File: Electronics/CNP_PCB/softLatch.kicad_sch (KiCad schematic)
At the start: 10 parts, among them Q2 Q_NMOS_GSD, Q3 Q_NMOS_GSD, Q5 Q_PMOS_GSD, SW1 SW_SPST

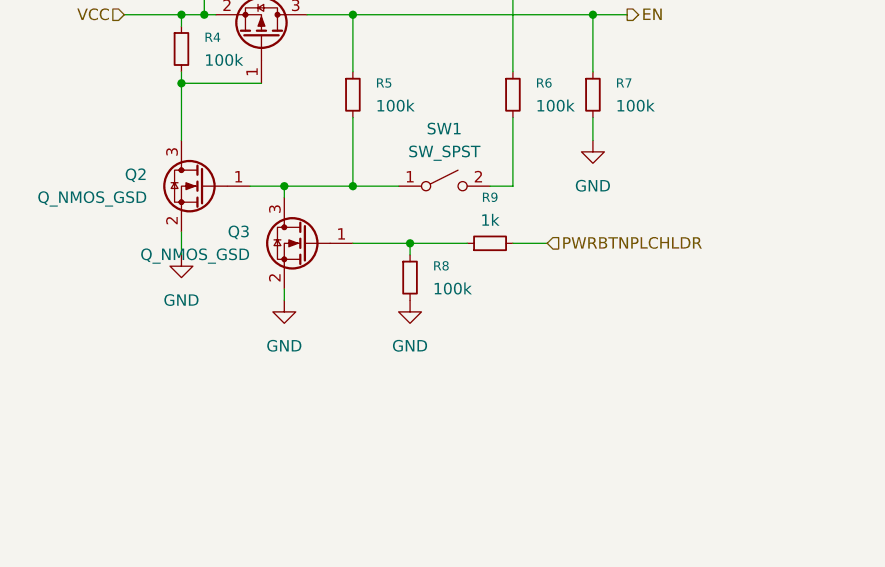
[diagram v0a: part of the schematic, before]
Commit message: finished softLatch circuit
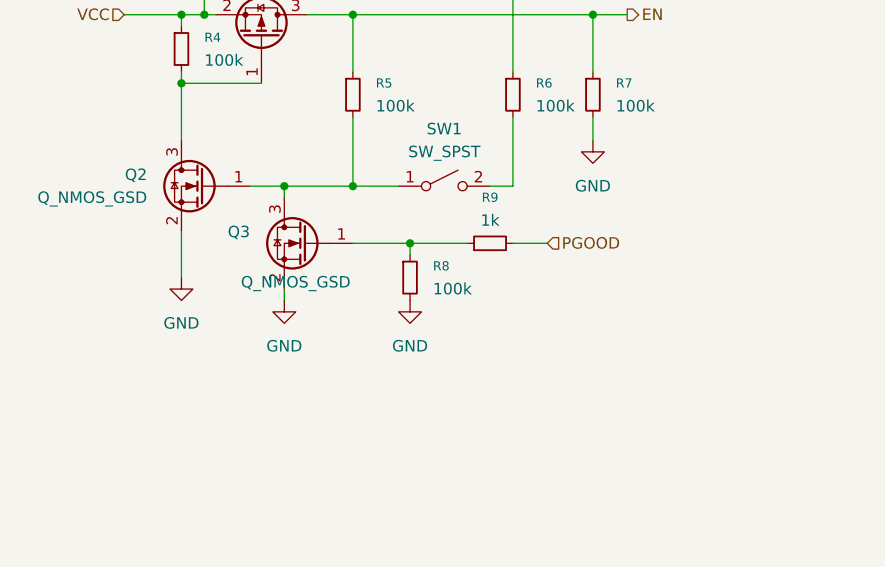
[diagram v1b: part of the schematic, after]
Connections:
- net PWRBTNPLCHLDR renamed PGOOD
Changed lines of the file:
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@@
 	(wire
 		(pts
-			(xy 137.16 76.2) (xy 137.16 73.66)
+			(xy 137.16 78.74) (xy 137.16 73.66)
 		)
 		(stroke
@@
 		)
 	)
-	(hierarchical_label "PWRBTNPLCHLDR"
+	(hierarchical_label "PGOOD"
 		(shape input)
 		(at 177.8 74.93 0)
@@
 		(on_board yes)
 		(dnp no)
-		(fields_autoplaced yes)
 		(property "Reference" "Q3"
 			(at 144.78 73.6599 0)
@@
 		)
 		(property "Value" "Q_NMOS_GSD"
-			(at 144.78 76.1999 0)
+			(at 155.956 79.248 0)
 			(effects
 				(font
@@
 	(symbol
 		(lib_id "power:GND")
-		(at 137.16 76.2 0)
+		(at 137.16 78.74 0)
 		(unit 1)
 		(exclude_from_sim no)
@@
 		(fields_autoplaced yes)
 		(property "Reference" "#PWR010"
-			(at 137.16 82.55 0)
+			(at 137.16 85.09 0)
 			(effects
 				(font
@@
 		)
 		(property "Value" "GND"
-			(at 137.16 81.28 0)
+			(at 137.16 83.82 0)
 			(effects
 				(font
@@
 		)
 		(property "Footprint" ""
-			(at 137.16 76.2 0)
+			(at 137.16 78.74 0)
 			(effects
 				(font
@@
 		)
 		(property "Datasheet" ""
-			(at 137.16 76.2 0)
+			(at 137.16 78.74 0)
 			(effects
 				(font
@@
 		)
 		(property "Description" "Power symbol creates a global label with name \"GND\" , ground"
-			(at 137.16 76.2 0)
-			(effects
-				(font
+			(at 137.16 78.74 0)
+			(effects
+				(font

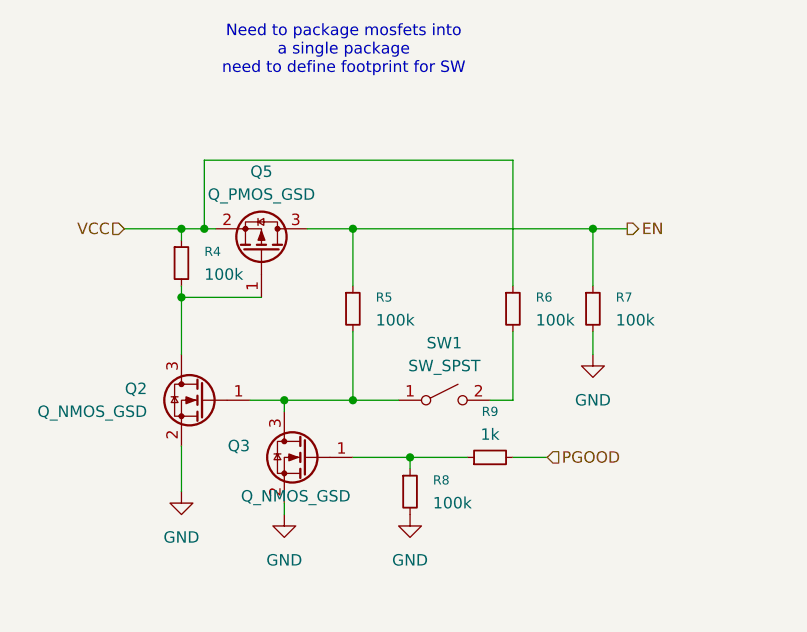
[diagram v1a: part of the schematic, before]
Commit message: added switch logic for emulating buttons
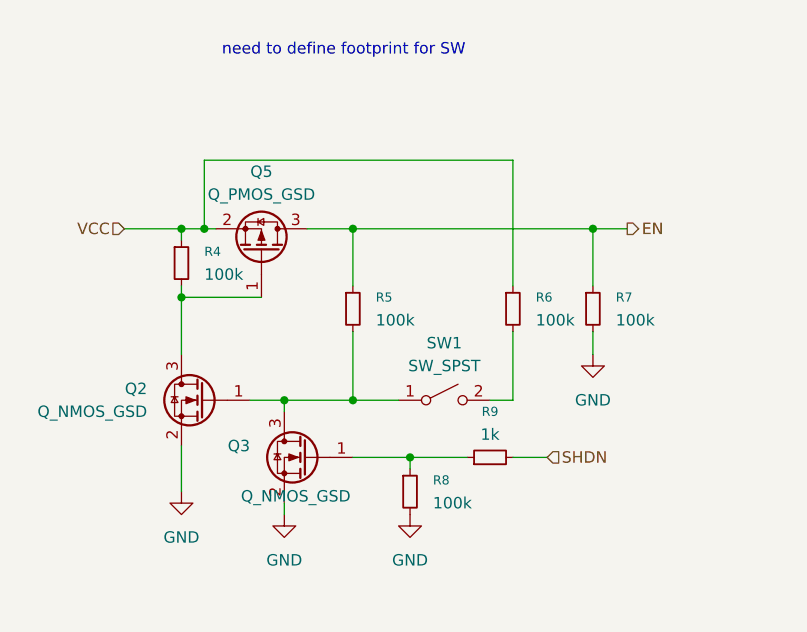
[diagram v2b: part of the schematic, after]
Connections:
- net PGOOD renamed SHDN
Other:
- note added: "need to define footprint for SW"
- note removed: "Need to package mosfets into a single package need to define footprint for SW"
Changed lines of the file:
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@@
 	(generator_version "9.0")
 	(paper "A4")
-	(text "Need to package mosfets into\na single package \nneed to define footprint for SW"
+	(text "need to define footprint for SW"
 		(exclude_from_sim no)
 		(at 155.194 29.718 0)
@@
 			"DgAAAAkS7AAAAJAgwQ4AAAAJEuwAAACQIMEOAAAACRLsAAAAkCDBDgAAAAkS7AAAAJAgwQ4AAAAJ"
 			"EuwAAACQIMEOAAAACRLsAAAAkCDBDgAAAAkS7AAAAJAgwQ4AAAAJ+l8K8UU2bGmH5gAAAABJRU5E"
-			"rkJggg=="
-		)
-	)
-	(hierarchical_label "PGOOD"
+			"rkJgggAAAAAAAAAAAAAAAAAAAAAAAAAAAAAAAAAAAAAAAAAAAAAAAAAAAAAAAAAAAAAAAAAAAAAA"
+			"AAAAAAAAAAAAAAAAAAAAAAAAAAAAAAAAAAAAAAAAAAAAAAAAAAAAAAAAAAAAAAAAAAAAAAAAAAAA"
+			"AAAAAAAAAAAAAAAAAAAAAAAAAAAAAAAAAAAAAAAAAAAAAAAAAAAAAAAAAAAAAAAAAAAAAAAAAAAA"
+			"AAAAAAAAAAAAAAAAAAAAAAAAAAAAAAAAAAAAAAAAAAAAAAAAAAAAAAAAAAAAAAAAAAAAAAAAAAAA"
+			"AAAAAAAAAAAAAAAAAAAAAAAAAAAAAAAAAAAAAAAAAAAAAAAAAAAAAAAAAAAAAAAAAAAAAAAAAAAA"
+			"AAAAAAAAAAAAAAAAAAAAAAAAAAAAAAAAAAAAAAAAAAAAAAAAAAAAAAAAAAAAAAAAAAAAAAAAAAAA"
+			"AAAAAAAAAAAAAAAAAAAAAAAAAAAAAAAAAAAAAAAAAAAAAAAAAAAAAAAAAAAAAAAAAAAAAAAAAAAA"
+			"AAAAAAAAAAAAAAAAAAAAAAAAAAAAAAAAAAAAAAAAAAAAAAAAAAAAAAAAAAAAAAAAAAAAAAAAAAAA"
+			"AAAAAAAAAAAAAAAAAAAAAAAAAAAAAAAAAAAAAAAAAAAAAAAAAAAAAAAAAAAAAAAAAAAAAAAAAAAA"
+			"AAAAAAAAAAAAAAAAAAAAAAAAAAAAAAAAAAAAAAAAAAAAAAAAAAAAAAAAAAAAAAAAAAAAAAAAAAAA"
+			"AAAAAAAAAAAAAAAAAAAAAAAAAAAAAAAAAAAAAAAAAAAAAAAAAAAAAAAAAAAAAAAAAAAAAAAAAAAA"
+			"AAAAAAAAAAAAAAAAAAAAAAAAAAAAAAAAAAAAAAAAAAAAAAAAAAAAAAAAAAAAAAAAAAAAAAAAAAAA"
+			"AAAAAAAAAAAAAAAAAAAAAAAAAAAAAAAAAAAAAAAAAAAAAAAAAAAAAAAAAAAAAAAAAAAAAAAAAAAA"
+			"AAAAAAAAAAAAAAAAAAAAAAAAAAAAAAAAAAAAAAAAAAAAAAAAAAAAAAAAAAAAAAAAAAAAAAAAAAAA"
+			"AAAAAAAAAAAAAAAAAAAAAAAAAAAAAAAAAAAAAAAAAAAAAAAAAAAAAAAAAAAAAAAAAAAAAAAAAAAA"
+			"AAAAAAAAAAAAAAAAAAAAAAAAAAAAAAAAAAAAAAAAAAAAAAAAAAAAAAAAAAAAAAAAAAAAAAAAAAAA"
+			"AAAAAAAAAAAAAAAAAAAAAAAAAAAAAAAAAAAAAAAAAAAAAAAAAAAAAAAAAAAAAAAAAAAAAAAAAAAA"
+			"AAAAAAAAAAAAAAAAAAAAAAAAAAAAAAAAAAAAAAAAAAAAAAAAAAAAAAAAAAAAAAAAAAAAAAAAAAAA"
+			"AAAAAHpic3ZkMGJ0bzRpekVwZU0yZTh0MzlaNlZwTThPUERadUZEOTEvNk1QUGJ2djRZZjNva1J0"
+			"Sm9TL0R1eHBpSHdpYzBhb3NJbzA1NmVHbEtSb1NGbEZXbEZXaElRUWVUQ2FXTjB4Z2k0dW45bjBJ"
+			"amk5aTRnUnJLbk9LTHdtZ21WQmtTbVAxeklWSDVFeFJSZ2NSK1dNbE9nSHU5VFdCVzVVU01sWmkr"
+			"b0E0blVjZU5saXRWZ0w2WndBYW1BTVVpRjJPR1JKV1ZPT2xBMERKV0NNRXBvNDNQQXAwQ1NQRWpP"
+			"NkhaWkcySTI1cERSYU5lWkxRdERBWkV4eElmRmtjMGVuKythZlBQOUtSK2ZjcTFiZDF0RUpqdU9m"
+			"dzF1TzkvVEhWTSsxTHJ5bnZYOEhTdGNETUkyaStuV2lKK2FjVnRJWDZ2MFZwVWlLdHZNaktaaVE4"
+			"VTFnMG94SHFKOHNGODI4OEE1YU5aeTVDbm5tRUZvUkxZRlcwTFFHWXRMbHhIUTZLTllZRGxNUDNH"
+			"TFFUODluWFc1a3JYRGFFQjJYTmtYSCtTdm13eWN4RXY2NXlUQTFPblhCMXFsYnB5NVl5RTZuUktj"
+			"czJEcGw2NVFGQ3pFZmZGTTM1WGxDbk5PMmpuTjJVVXA0bTJPMG8wZHZzV284NnRvaU9BY1hLWXQw"
+			"ZHNERzBSaDRjYW5lclBwMTZYTzVoczF2WVBrYWZoRE9Kc2RkREdkRENqaWJjbHNwZC9sbXloeG1B"
+			"UDFUeEVTSW40bksrQm5NWjhYa2ZKWk9XM0tKTGNac01Ua1RZMFYrd3M1Y1NvYjJhSUFuZUE5andR"
+			"TGdSb2VMMjR6QWVUM21ObTdCQzNJZUF6TmNLekp1WTZCVzVEMjZqTVlkck9XNnpHNFlyTXNOc1Zr"
+			"UGsrVVpzeFdHdU1HY09LMXNEV2tSQUVaT2N5VVlWSnNtNUZyaEF4MmQ5RVpSbE5iVDdmdjJTMmZY"
+			"STd2MS9aWitUMXJjZncwOS9TMXByNExjb004enpNNHRnekE3WDRuVGNGcVIyNHFtY3lqT1NvenMw"
+			"UnQrQUNuTndEc3lpa2p6UGJBdFNmb3IrWTJTdVRjYWs2ZHdrdWtQVHpySktEdzJyejg4ak1JK2hl"
+			"bE5vRDhjNkpXSHlTTFJVWGVZTE9veGFmbXEwVE9ianNHcm9IdmVrR1J2T0JwZXRuSVlhMWJGQndq"
+			"QTNHc1REWXlxU1pyTTQ2VzZ5b1FZZUR4dEIydUcxUXdiNWtteVpjWktIeFdEZnJ6QjdYRjdsQnRB"
+			"NVRRTVE1VlRNd3pURllmS2hNcFl6YkNVeG8wSXkwby85Z1Q5NERZMkl2ekZuK0xoT3NpYjZCa0xs"
+			"cU53Uw=="
+		)
+	)
+	(hierarchical_label "SHDN"
 		(shape input)
 		(at 177.8 74.93 0)
